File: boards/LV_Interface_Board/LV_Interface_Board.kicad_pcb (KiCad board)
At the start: 2 copper layers, 136 x 100 mm, 23 parts, among them J1 Ampseal_35, J2 Ampseal_35, J3 micromatch_male_6, J4 micromatch_male_20, J5 micromatch_male_20, J6 micromatch_male_12, J7 micromatch_male_18, J8 micromatch_male_20, J9 micromatch_male_20, SW1 3P4T_rotary_switch, U1 RJ45_VT, U2 HT16K33

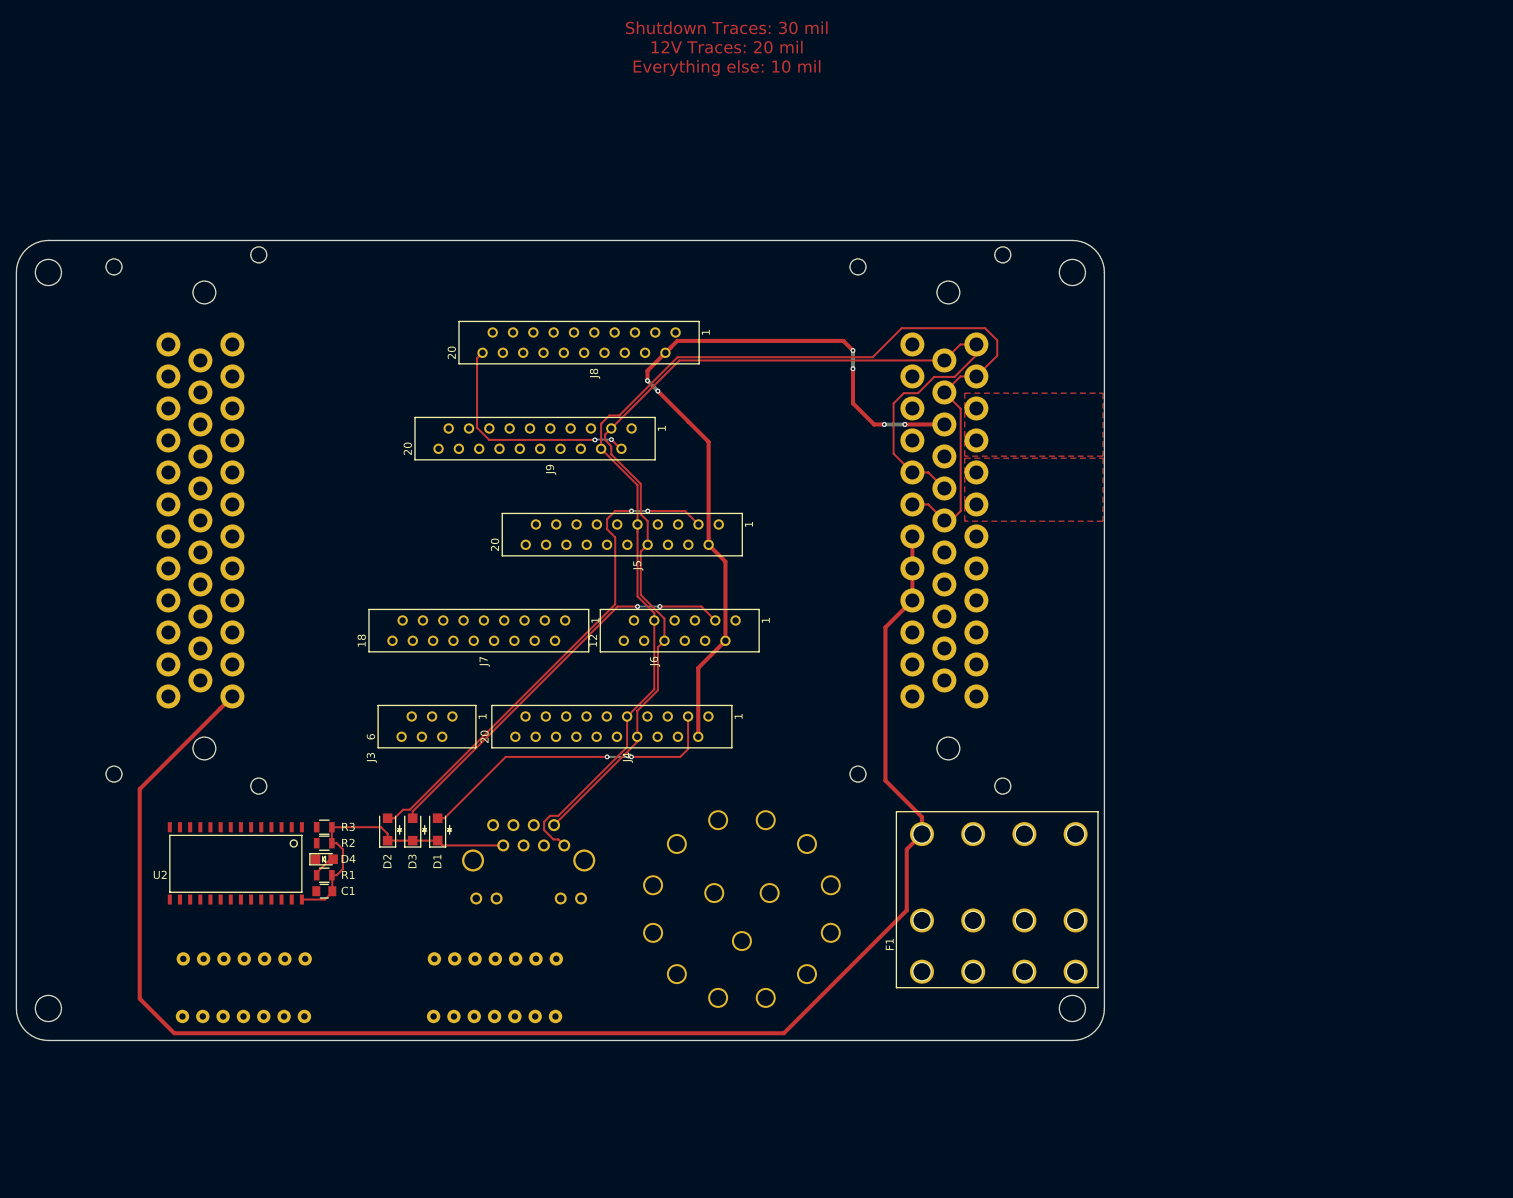
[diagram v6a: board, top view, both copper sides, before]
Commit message: improved routing
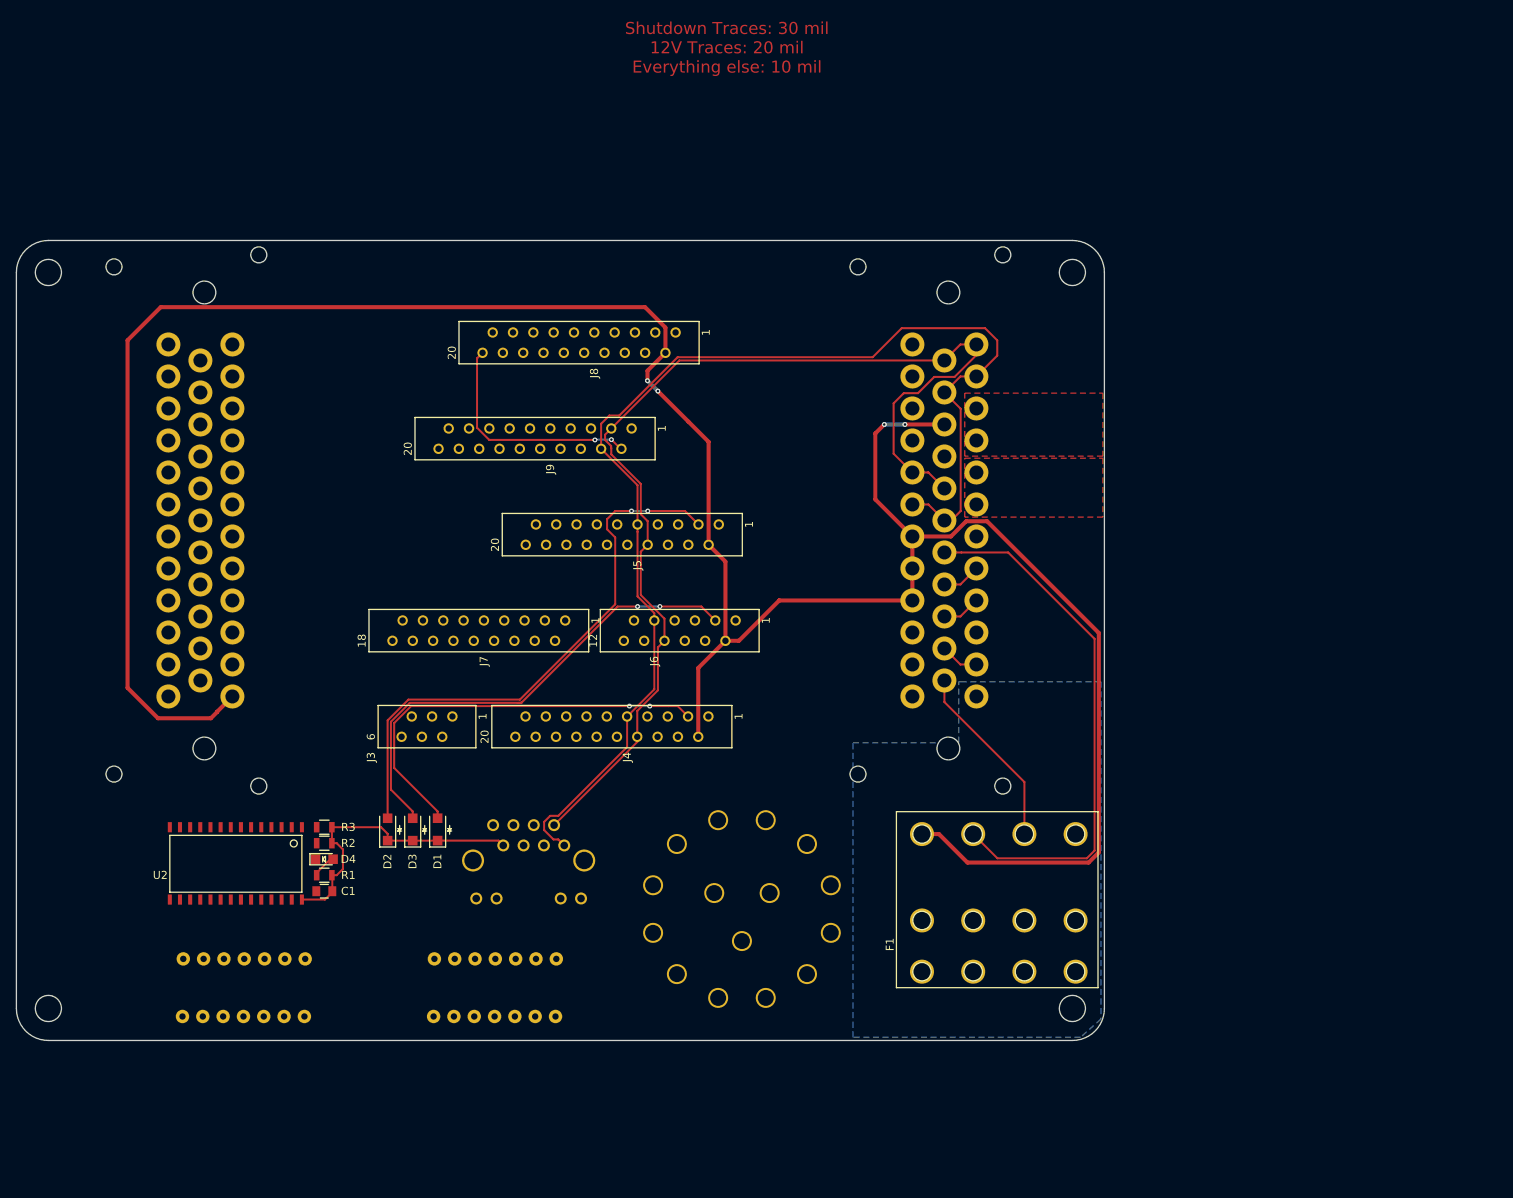
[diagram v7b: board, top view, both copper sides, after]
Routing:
- net /COOLING_PUMP_12V_FUSED: track 0.00 -> 66.5 mm
- net /12V: track 295.5 -> 325.6 mm, vias 6 -> 4
- net /MAIN_SHUTDOWN_FUSE: track 0.00 -> 23.3 mm
- net Net-(D1-Pad2): track 39.0 -> 52.3 mm
- net Net-(D3-Pad2): track 50.0 -> 60.9 mm
- net Net-(D2-Pad2): track 63.1 -> 70.3 mm
- net /TSMS: track 0.00 -> 4.83 mm
- net /LEFT_E-STOP: track 0.00 -> 4.83 mm
- net /HVD: track 0.00 -> 4.83 mm
- added copper zone on B.Cu, net /GLVMS

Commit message: improved routing
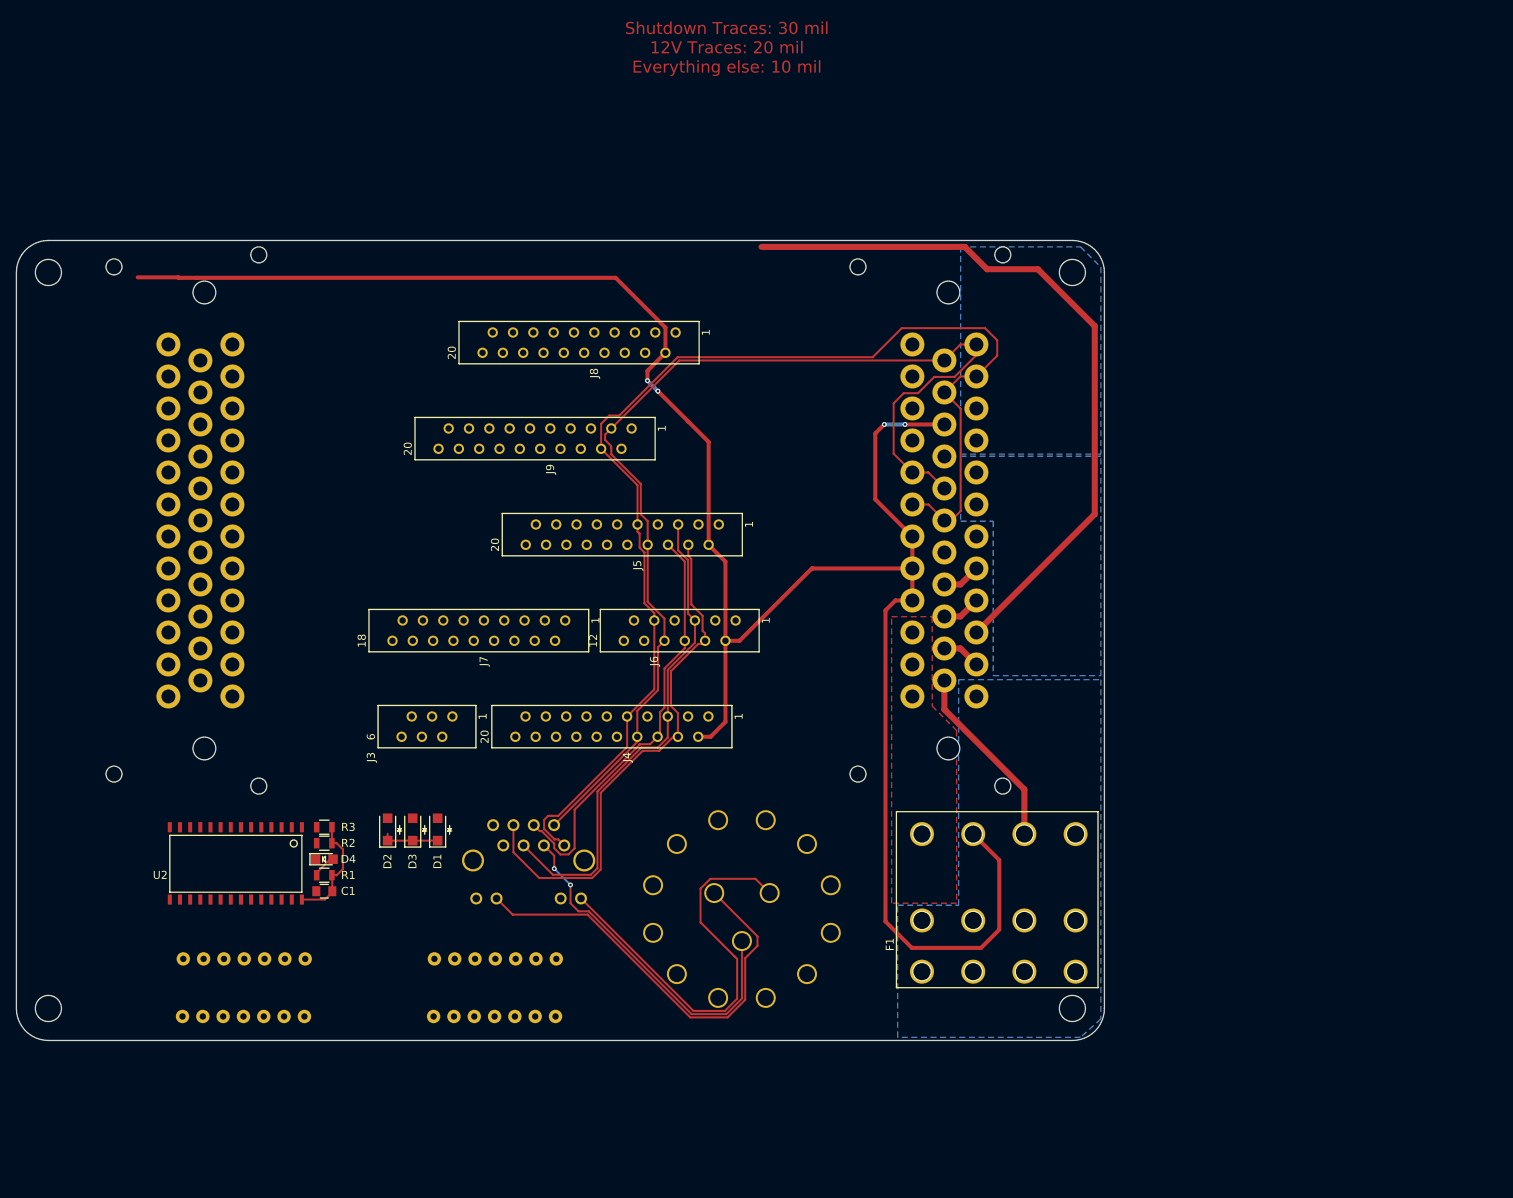
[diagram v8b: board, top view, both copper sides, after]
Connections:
- F1 pad 2: /12V -> /COOLING_PUMP_12V_FUSED
- F1 pad 4: /COOLING_PUMP_12V_FUSED -> /12V
- J1 pad 10: /BRAKE_LIGHT_LSD -> /COOLING_PUMP_12V_FUSED
- J1 pad 11: /BRAKE_SWITCH+ -> /COOLING_PUMP_12V_FUSED
- J1 pad 12: /BRAKE_SWITCH- -> /COOLING_PUMP_12V_FUSED
- J1 pad 19: /COOLING_PUMP_12V_FUSED -> /BRAKE_LIGHT_LSD
- J2 pad 11: Net-(J2-Pad11) -> /BRAKE_SWITCH+
- J2 pad 12: Net-(J2-Pad12) -> /BRAKE_SWITCH-
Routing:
- net /RIGHT_E-STOP: track 0.00 -> 90.2 mm
- net Net-(D2-Pad2): track 70.3 -> 0.00 mm, vias 2 -> 0
- net /12V: track 325.6 -> 258.7 mm
- net /COOLING_PUMP_12V_FUSED: track 66.5 -> 0.00 mm
- net /MOSI: track 0.00 -> 65.5 mm
- net /MISO: track 0.00 -> 61.2 mm
- net Net-(D3-Pad2): track 60.9 -> 0.00 mm, vias 2 -> 0
- net /LED1: track 0.00 -> 54.4 mm
- net /SCK: track 0.00 -> 52.5 mm
- net Net-(D1-Pad2): track 52.3 -> 0.00 mm, vias 2 -> 0
- net /LED2: track 0.00 -> 51.7 mm
- net /RESET: track 0.00 -> 43.8 mm, vias 0 -> 2
- net /5V_DATA: track 28.8 -> 0.00 mm, vias 2 -> 0
- net /5V: track 37.0 -> 21.3 mm
- net /CAN_HIGH: track 138.0 -> 137.3 mm
- added copper zone on B.Cu, net /BAT+
- added copper zone on B.Cu, net /BREAKER
- added copper zone on F.Cu, net /COOLING_PUMP_12V_FUSED
- removed copper zone on F.Cu, net /BAT+
- removed copper zone on F.Cu, net /BREAKER
